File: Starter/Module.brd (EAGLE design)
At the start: 25.4 x 25.4 mm, 3 parts

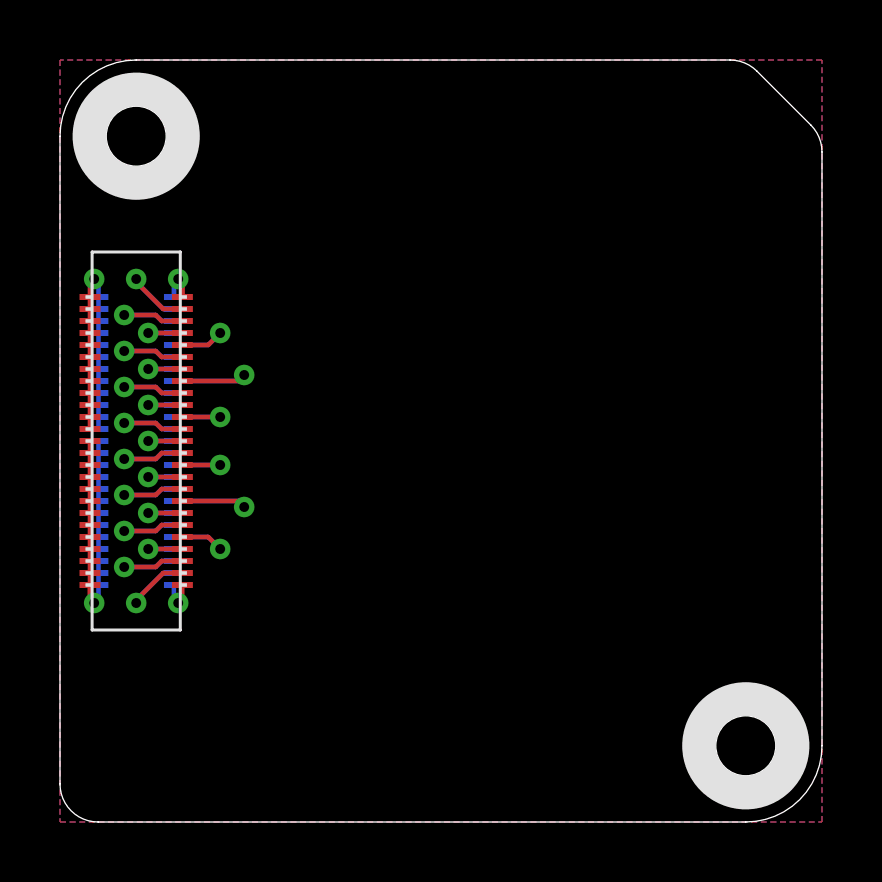
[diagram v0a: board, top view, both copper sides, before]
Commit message: Updated Starter Module for updated holes, support for external power, and updated header from library.
Signed-off-by: Cruz Monrreal II <Cruz.Monrreal@gmail.com>
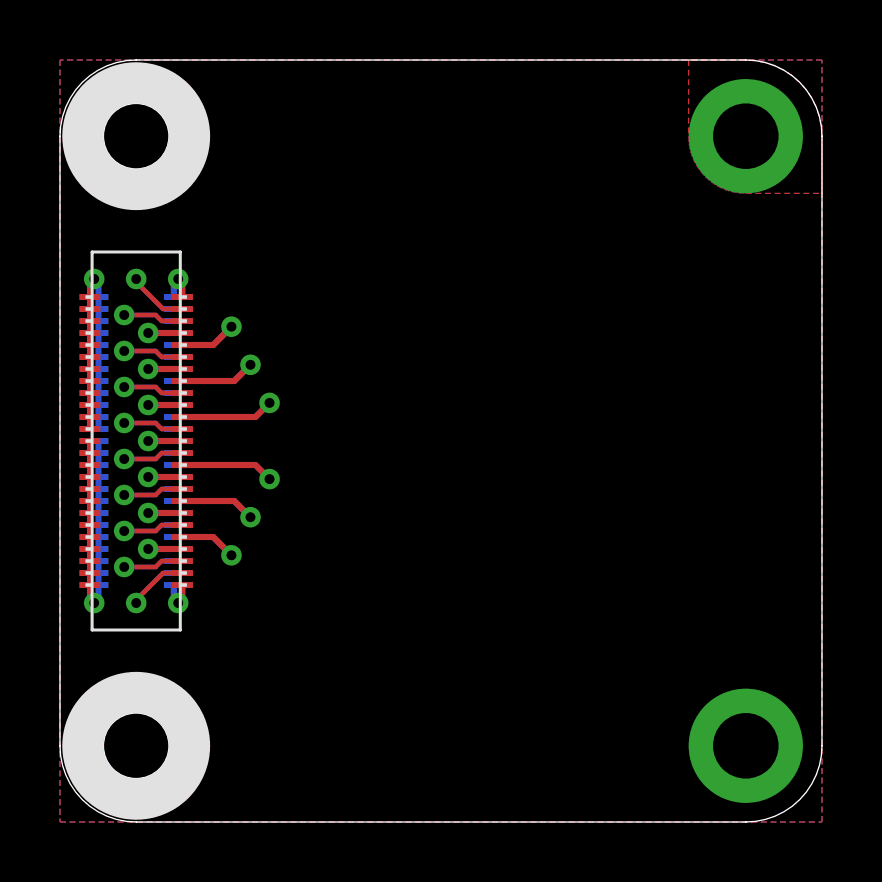
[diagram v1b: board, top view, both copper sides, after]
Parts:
- U$3, U$4: value HOLE.2MM -> HOLE.#2; device .screw_holes:2MM -> .screw_holes:#2
- moved U$3 20.3 mm to (2.54, 2.54)
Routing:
- added copper zone on layer 1, net VIN
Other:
- outline, holes or cut-outs redrawn
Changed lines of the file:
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@@
 <layers>
 <layer number="1" name="Top" color="4" fill="1" visible="yes" active="yes"/>
+<layer number="2" name="Route2" color="1" fill="3" visible="no" active="no"/>
+<layer number="3" name="Route3" color="4" fill="3" visible="no" active="no"/>
+<layer number="4" name="Route4" color="1" fill="4" visible="no" active="no"/>
+<layer number="5" name="Route5" color="4" fill="4" visible="no" active="no"/>
+<layer number="6" name="Route6" color="1" fill="8" visible="no" active="no"/>
+<layer number="7" name="Route7" color="4" fill="8" visible="no" active="no"/>
+<layer number="8" name="Route8" color="1" fill="2" visible="no" active="no"/>
+<layer number="9" name="Route9" color="4" fill="2" visible="no" active="no"/>
+<layer number="10" name="Route10" color="1" fill="7" visible="no" active="no"/>
+<layer number="11" name="Route11" color="4" fill="7" visible="no" active="no"/>
+<layer number="12" name="Route12" color="1" fill="5" visible="no" active="no"/>
+<layer number="13" name="Route13" color="4" fill="5" visible="no" active="no"/>
+<layer number="14" name="Route14" color="1" fill="6" visible="no" active="no"/>
+<layer number="15" name="Route15" color="4" fill="6" visible="no" active="no"/>
 <layer number="16" name="Bottom" color="1" fill="1" visible="yes" active="yes"/>
 <layer number="17" name="Pads" color="2" fill="1" visible="yes" active="yes"/>
@@
 <layer number="24" name="bOrigins" color="15" fill="1" visible="yes" active="yes"/>
 <layer number="25" name="tNames" color="7" fill="1" visible="yes" active="yes"/>
-<layer number="26" name="bNames" color="7" fill="1" visible="yes" active="yes"/>
-<layer number="27" name="tValues" color="7" fill="1" visible="yes" active="yes"/>
-<layer number="28" name="bValues" color="7" fill="1" visible="yes" active="yes"/>
+<layer number="26" name="bNames" color="7" fill="1" visible="no" active="yes"/>
+<layer number="27" name="tValues" color="7" fill="1" visible="no" active="yes"/>
+<layer number="28" name="bValues" color="7" fill="1" visible="no" active="yes"/>
 <layer number="29" name="tStop" color="7" fill="3" visible="no" active="yes"/>
 <layer number="30" name="bStop" color="7" fill="6" visible="no" active="yes"/>
@@
 <board>
 <plain>
-<wire x1="0" y1="22.86" x2="0" y2="1.27" width="0" layer="20"/>
-<wire x1="0" y1="1.27" x2="1.27" y2="0" width="0" layer="20" curve="90"/>
-<wire x1="1.27" y1="0" x2="22.86" y2="0" width="0" layer="20"/>
+<wire x1="0" y1="22.86" x2="0" y2="2.54" width="0" layer="20"/>
+<wire x1="0" y1="2.54" x2="2.54" y2="0" width="0" layer="20" curve="90"/>
+<wire x1="2.54" y1="0" x2="22.86" y2="0" width="0" layer="20"/>
 <wire x1="22.86" y1="0" x2="25.4" y2="2.54" width="0" layer="20" curve="90"/>
-<wire x1="25.4" y1="2.54" x2="25.4" y2="22.33395" width="0" layer="20"/>
-<wire x1="25.4" y1="22.33395" x2="25.028025" y2="23.231975" width="0" layer="20" curve="45"/>
-<wire x1="25.028025" y1="23.231975" x2="23.231975" y2="25.028025" width="0" layer="20"/>
-<wire x1="23.231975" y1="25.028025" x2="22.33395" y2="25.4" width="0" layer="20" curve="45"/>
-<wire x1="22.33395" y1="25.4" x2="2.54" y2="25.4" width="0" layer="20"/>
+<wire x1="25.4" y1="2.54" x2="25.4" y2="22.86" width="0" layer="20"/>
+<wire x1="25.4" y1="22.86" x2="22.86" y2="25.4" width="0" layer="20" curve="90"/>
+<wire x1="22.86" y1="25.4" x2="2.54" y2="25.4" width="0" layer="20"/>
 <wire x1="2.54" y1="25.4" x2="0" y2="22.86" width="0" layer="20" curve="90"/>
 <text x="12.7" y="1.27" size="1.016" layer="52" font="vector" ratio="12" rot="MR0" align="bottom-center">AnomalousMaker.com</text>
@@
 <vertex x="31.62808125" y="10.3298"/>
 </polygon>
-<text x="0.635" y="1.27" size="1.016" layer="52" font="vector" ratio="12" rot="MR0" align="bottom-right">v1</text>
+<text x="0.635" y="6.35" size="1.016" layer="52" font="vector" ratio="12" rot="MR0" align="top-right">v1</text>
+<polygon width="0.254" layer="29">
+<vertex x="20.955" y="25.4"/>
+<vertex x="20.955" y="22.86" curve="90"/>
+<vertex x="22.86" y="20.955"/>
+<vertex x="25.4" y="20.955"/>
+<vertex x="25.4" y="22.86" curve="90"/>
+<vertex x="22.86" y="25.4"/>
+</polygon>
+<polygon width="0.254" layer="29">
+<vertex x="25.4" y="4.445"/>
+<vertex x="22.86" y="4.445" curve="90"/>
+<vertex x="20.955" y="2.54"/>
+<vertex x="20.955" y="0"/>
+<vertex x="22.86" y="0" curve="90"/>
+<vertex x="25.4" y="2.54"/>
+</polygon>
 </plain>
 <attributes>
@@
 </autorouter>
 <elements>
-<element name="U$4" library=".screw_holes" package="2MM" value="HOLE.2MM" x="2.54" y="22.86" rot="R90"/>
-<element name="U$3" library=".screw_holes" package="2MM" value="HOLE.2MM" x="22.86" y="2.54" rot="R90"/>
+<element name="U$4" library=".screw_holes" package="#2" value="HOLE.#2" x="2.54" y="22.86" rot="R90"/>
+<element name="U$3" library=".screw_holes" package="#2" value="HOLE.#2" x="2.54" y="2.54" rot="R90"/>
 <element name="U$2" library="thinkmaketest" package="ROOT1.BOTH" value="ROOT1.BOTH" x="0" y="0"/>
 </elements>
@@
 <contactref element="U$2" pad="GND@26"/>
 <contactref element="U$2" pad="GND@VIA"/>
-<wire x1="0.995" y1="7.9" x2="1" y2="7.9" width="0" layer="19" extent="1-1"/>
-<wire x1="1.285" y1="7.9" x2="1.28" y2="7.9" width="0" layer="19" extent="16-16"/>
+<via x="22.86" y="2.54" extent="1-16" drill="2.1844" diameter="3.81"/>
 </signal>
 <signal name="N$30">
@@
 <contactref element="U$2" pad="MOSI"/>
 <contactref element="U$2" pad="MOSI@VIA"/>
-<wire x1="3.595" y1="15.9" x2="3.795" y2="15.9" width="0" layer="19" extent="16-16"/>
 </signal>
 <signal name="N$13">
@@
 <contactref element="U$2" pad="ADC0"/>
 <contactref element="U$2" pad="ADC0@1"/>
-<wire x1="3.795" y1="17.5" x2="3.8" y2="17.5" width="0" layer="19" extent="16-16"/>
-<wire x1="4.08" y1="17.5" x2="4.085" y2="17.5" width="0" layer="19" extent="1-1"/>
 </signal>
 <signal name="N$17">
@@
 <contactref element="U$2" pad="WAKE"/>
 </signal>
+<signal name="VIN">
+<via x="22.86" y="22.86" extent="1-16" drill="2.1844" diameter="3.81"/>
+<polygon width="0.254" layer="1">
+<vertex x="20.955" y="25.4"/>
+<vertex x="20.955" y="22.86" curve="90"/>
+<vertex x="22.86" y="20.955"/>
+<vertex x="25.4" y="20.955"/>
+<vertex x="25.4" y="22.86" curve="90"/>
+<vertex x="22.86" y="25.4"/>
+</polygon>
+</signal>
 </signals>
